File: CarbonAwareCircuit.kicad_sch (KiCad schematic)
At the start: 2 parts, among them J1 USB_C_Receptacle_USB2.0_14P, U2 ESP32-C3-WROOM-02

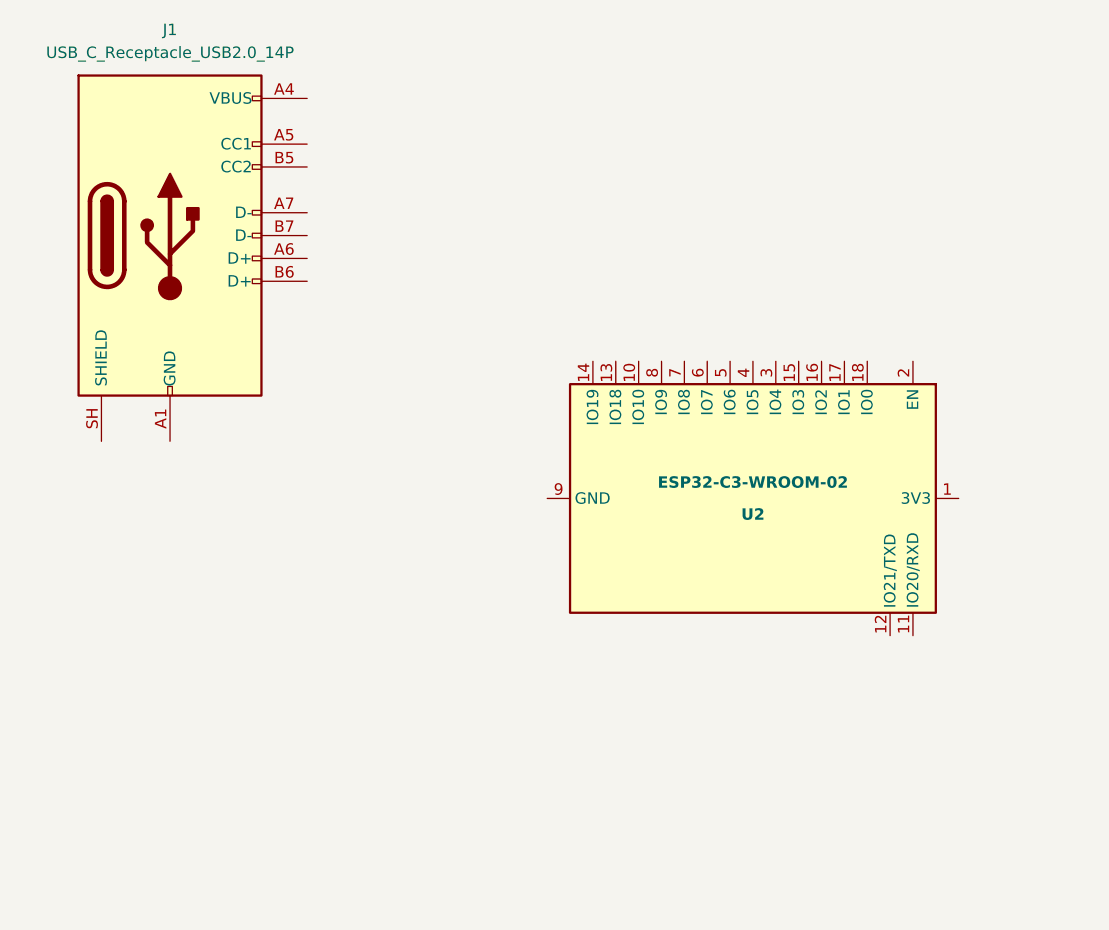
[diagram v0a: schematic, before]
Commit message: connected input port & ERR_LED
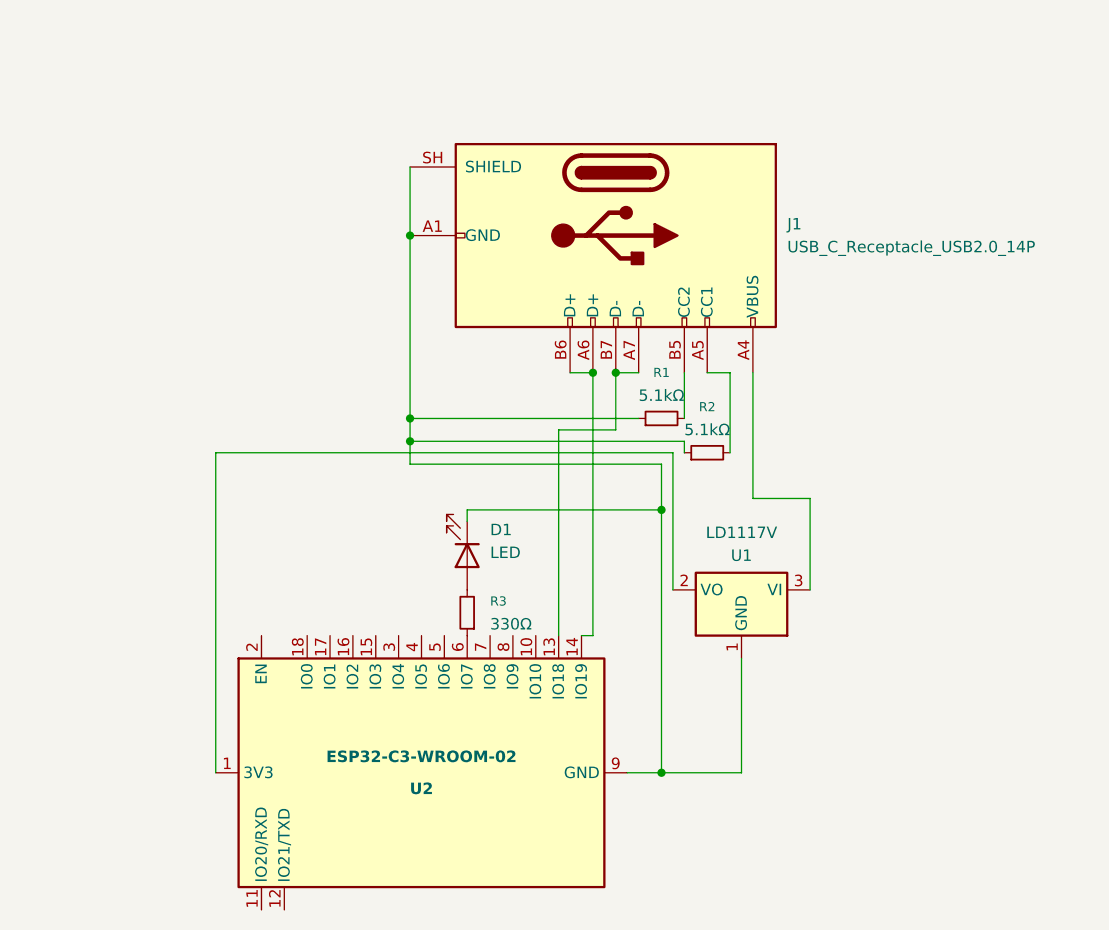
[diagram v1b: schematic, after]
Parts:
- added D1: LED, symbol Device:LED
- added R1, R2: 5.1kΩ, symbol Device:R_Small
- added R3: 330Ω, symbol Device:R_Small
- added U1: LD1117V, Package_TO_SOT_THT:TO-220-3_Vertical, symbol Regulator_Linear:LD1117V
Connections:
- net at U2.1 (3V3): now also U1.2 (VO)
- net at U2.13 (IO18): now also J1.A7 (D-), J1.B7 (D-)
- net at U2.14 (IO19): now also J1.A6 (D+), J1.B6 (D+)
- net at U2.19 (GND), U2.9 (GND): now also J1.A1 (GND), J1.A12 (GND), J1.B1 (GND), J1.B12 (GND), J1.SH (SHIELD), D1.1 (K), R1.1, R2.1, U1.1 (GND)
- net at U2.6 (IO7): now also R3.1
- net at J1.A4 (VBUS), J1.A9 (VBUS), J1.B4 (VBUS)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: now also U1.3 (VI)
- net at J1.A5 (CC1): now also R2.2
- net at J1.B5 (CC2): now also R1.2
- new net: D1.2 (A), R3.2
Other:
- moved on the sheet: J1, U2
